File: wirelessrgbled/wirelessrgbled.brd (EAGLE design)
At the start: 38.1 x 50.8 mm, 38 parts, among them J1 1X2-3.5MM, J2 1X2-3.5MM

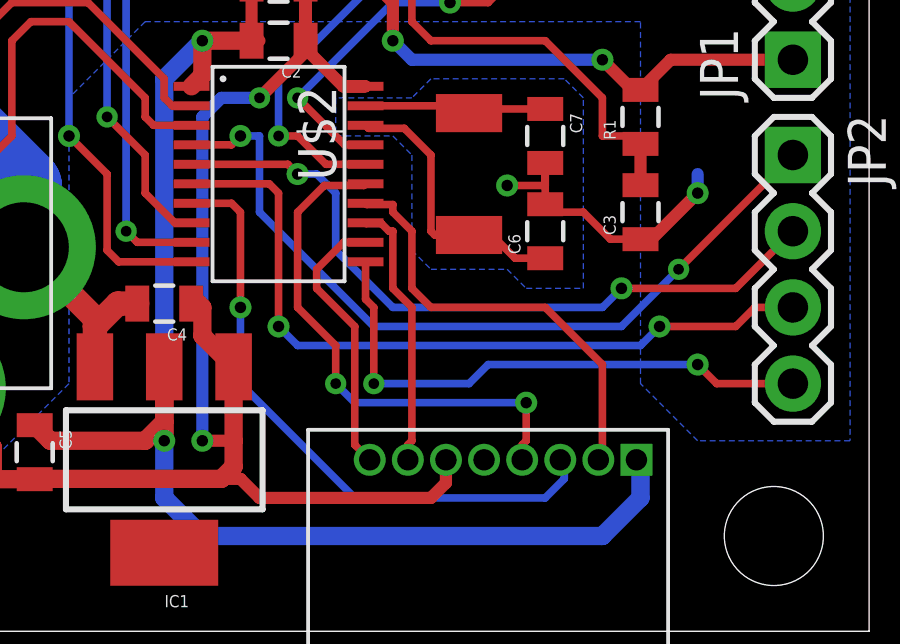
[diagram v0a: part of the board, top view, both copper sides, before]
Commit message: Updating wirelessrgbled to v1.1
Adding msp430-cc2500 v1.1
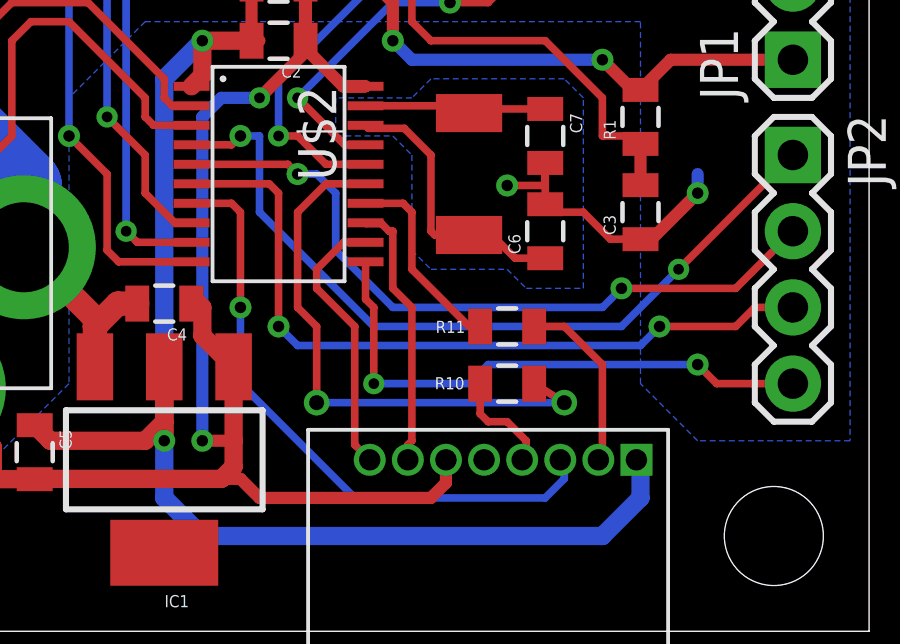
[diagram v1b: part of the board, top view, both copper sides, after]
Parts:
- added R10, R11: 0, SparkFun:0805
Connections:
- new net N$7: R10.2, U$2.15
- new net N$9: R11.2, U$2.14
- net SI: now also R11.1; no longer U$2.14
- net SO: now also R10.1; no longer U$2.15
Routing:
- net N$7: track 0.00 -> 18.7 mm, vias 0 -> 2
- net SO: track 17.5 -> 3.60 mm, vias 2 -> 0
- net SI: track 14.6 -> 6.03 mm
- net N$9: track 0.00 -> 6.64 mm
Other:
- board text added: "wirelessrgbled v1.1"
- board text removed: "wirelessrgbled v1.0"
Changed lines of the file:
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@@
 <text x="28.575" y="47.625" size="1.778" layer="25">12v</text>
 <text x="33.02" y="37.465" size="1.778" layer="26" font="vector" rot="MR0">alvarop.com</text>
-<text x="33.02" y="35.56" size="1.778" layer="26" font="vector" rot="MR0">wirelessrgbled v1.0</text>
+<text x="33.02" y="35.56" size="1.778" layer="26" font="vector" rot="MR0">wirelessrgbled v1.1</text>
 </plain>
 <attributes>
@@
 <element name="JP2" library="SparkFun" package="1X04" value="" x="35.56" y="15.875" rot="R270"/>
 <element name="LOGO1" library="ohw-logo" package="OSHW_10X200_NOTEXT" value="OSHW_LOGO_10MILX0200-NT" x="33.02" y="40.005" rot="MR0"/>
+<element name="R10" library="SparkFun" package="0805" value="0" x="26.035" y="8.255" smashed="yes">
+<attribute name="NAME" x="23.622" y="8.0645" size="0.4064" layer="25"/>
+<attribute name="VALUE" x="25.908" y="8.128" size="0.4064" layer="27"/>
+</element>
+<element name="R11" library="SparkFun" package="0805" value="0" x="26.035" y="10.16" smashed="yes" rot="R180">
+<attribute name="NAME" x="24.638" y="10.3505" size="0.4064" layer="25" rot="R180"/>
+<attribute name="VALUE" x="26.162" y="10.287" size="0.4064" layer="27" rot="R180"/>
+</element>
 </elements>
 <signals>
@@
 </signal>
 <signal name="SI">
-<contactref element="U$2" pad="14"/>
 <contactref element="U$3" pad="2"/>
-<wire x1="29.075" y1="5.715" x2="29.21" y2="5.85" width="0.254" layer="1" curve="90"/>
-<wire x1="29.21" y1="5.85" x2="29.21" y2="8.89" width="0.254" layer="1"/>
-<wire x1="29.21" y1="8.89" x2="27.305" y2="10.795" width="0.254" layer="1"/>
-<wire x1="27.305" y1="10.795" x2="23.495" y2="10.795" width="0.254" layer="1"/>
-<wire x1="23.495" y1="10.795" x2="22.86" y2="11.43" width="0.254" layer="1"/>
-<wire x1="22.86" y1="11.43" x2="22.86" y2="13.335" width="0.254" layer="1"/>
-<wire x1="22.86" y1="13.335" x2="22.225" y2="13.97" width="0.254" layer="1"/>
-<wire x1="22.225" y1="13.97" x2="22.225" y2="14.224" width="0.254" layer="1"/>
-<wire x1="22.225" y1="14.224" x2="21.356" y2="14.224" width="0.254" layer="1"/>
-<wire x1="21.356" y1="14.224" x2="21.315" y2="14.265" width="0.254" layer="1"/>
+<contactref element="R11" pad="1"/>
+<wire x1="26.935" y1="10.16" x2="27.94" y2="10.16" width="0.254" layer="1"/>
+<wire x1="27.94" y1="10.16" x2="29.21" y2="8.89" width="0.254" layer="1"/>
+<wire x1="29.21" y1="8.89" x2="29.21" y2="5.85" width="0.254" layer="1"/>
+<wire x1="29.21" y1="5.85" x2="29.075" y2="5.715" width="0.254" layer="1"/>
 </signal>
 <signal name="SCLK">
@@
 </signal>
 <signal name="SO">
-<contactref element="U$2" pad="15"/>
 <contactref element="U$3" pad="4"/>
-<wire x1="26.535" y1="5.715" x2="26.535" y2="6.215" width="0.254" layer="1"/>
-<wire x1="26.535" y1="6.215" x2="26.67" y2="6.35" width="0.254" layer="1"/>
-<wire x1="26.67" y1="6.35" x2="26.67" y2="7.62" width="0.254" layer="1"/>
-<via x="26.67" y="7.62" extent="1-16" drill="0.381"/>
-<wire x1="26.67" y1="7.62" x2="20.955" y2="7.62" width="0.254" layer="16"/>
-<wire x1="20.955" y1="7.62" x2="20.32" y2="8.255" width="0.254" layer="16"/>
-<via x="20.32" y="8.255" extent="1-16" drill="0.3556"/>
-<wire x1="20.32" y1="8.255" x2="20.32" y2="9.525" width="0.254" layer="1"/>
-<wire x1="20.32" y1="9.525" x2="19.05" y2="10.795" width="0.254" layer="1"/>
-<wire x1="19.05" y1="10.795" x2="19.05" y2="13.97" width="0.254" layer="1"/>
-<wire x1="19.05" y1="13.97" x2="19.939" y2="14.859" width="0.254" layer="1"/>
-<wire x1="19.939" y1="14.859" x2="21.259" y2="14.859" width="0.254" layer="1"/>
-<wire x1="21.259" y1="14.859" x2="21.315" y2="14.915" width="0.254" layer="1"/>
+<contactref element="R10" pad="1"/>
+<wire x1="25.135" y1="8.255" x2="25.135" y2="7.25" width="0.254" layer="1"/>
+<wire x1="25.135" y1="7.25" x2="25.4" y2="6.985" width="0.254" layer="1"/>
+<wire x1="25.4" y1="6.985" x2="26.035" y2="6.985" width="0.254" layer="1"/>
+<wire x1="26.035" y1="6.985" x2="26.67" y2="6.35" width="0.254" layer="1"/>
+<wire x1="26.67" y1="6.35" x2="26.67" y2="5.85" width="0.254" layer="1"/>
+<wire x1="26.67" y1="5.85" x2="26.535" y2="5.715" width="0.254" layer="1"/>
 </signal>
 <signal name="GDO0">
@@
 <wire x1="33.02" y1="8.255" x2="35.56" y2="8.255" width="0.254" layer="1"/>
 </signal>
+<signal name="N$7">
+<contactref element="R10" pad="2"/>
+<contactref element="U$2" pad="15"/>
+<wire x1="21.315" y1="14.915" x2="19.995" y2="14.915" width="0.254" layer="1"/>
+<wire x1="19.995" y1="14.915" x2="19.05" y2="13.97" width="0.254" layer="1"/>
+<wire x1="19.05" y1="13.97" x2="19.05" y2="10.795" width="0.254" layer="1"/>
+<wire x1="19.05" y1="10.795" x2="19.685" y2="10.16" width="0.254" layer="1"/>
+<wire x1="19.685" y1="10.16" x2="19.685" y2="7.62" width="0.254" layer="1"/>
+<via x="19.685" y="7.62" extent="1-16" drill="0.5" diameter="0.254"/>
+<wire x1="19.685" y1="7.62" x2="27.94" y2="7.62" width="0.254" layer="16"/>
+<via x="27.94" y="7.62" extent="1-16" drill="0.5"/>
+<wire x1="27.94" y1="7.62" x2="26.935" y2="8.255" width="0.254" layer="1"/>
+</signal>
+<signal name="N$9">
+<contactref element="R11" pad="2"/>
+<contactref element="U$2" pad="14"/>
+<wire x1="21.315" y1="14.265" x2="22.565" y2="14.265" width="0.254" layer="1"/>
+<wire x1="22.565" y1="14.265" x2="22.86" y2="13.97" width="0.254" layer="1"/>
+<wire x1="22.86" y1="13.97" x2="22.86" y2="12.065" width="0.254" layer="1"/>
+<wire x1="22.86" y1="12.065" x2="24.765" y2="10.16" width="0.254" layer="1"/>
+<wire x1="24.765" y1="10.16" x2="25.135" y2="10.16" width="0.254" layer="1"/>
+</signal>
 </signals>
